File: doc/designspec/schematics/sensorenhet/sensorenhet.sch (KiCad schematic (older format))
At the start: 10 parts, among them IC1 ATMEGA1284P-P, U1 IQEXO-3, U2 Terminator-CTRL, U3 USB-UART, U4 Lidar_Lite_v2, U5 IR-Sensor, U6 IR-Sensor, U7 IR-Sensor

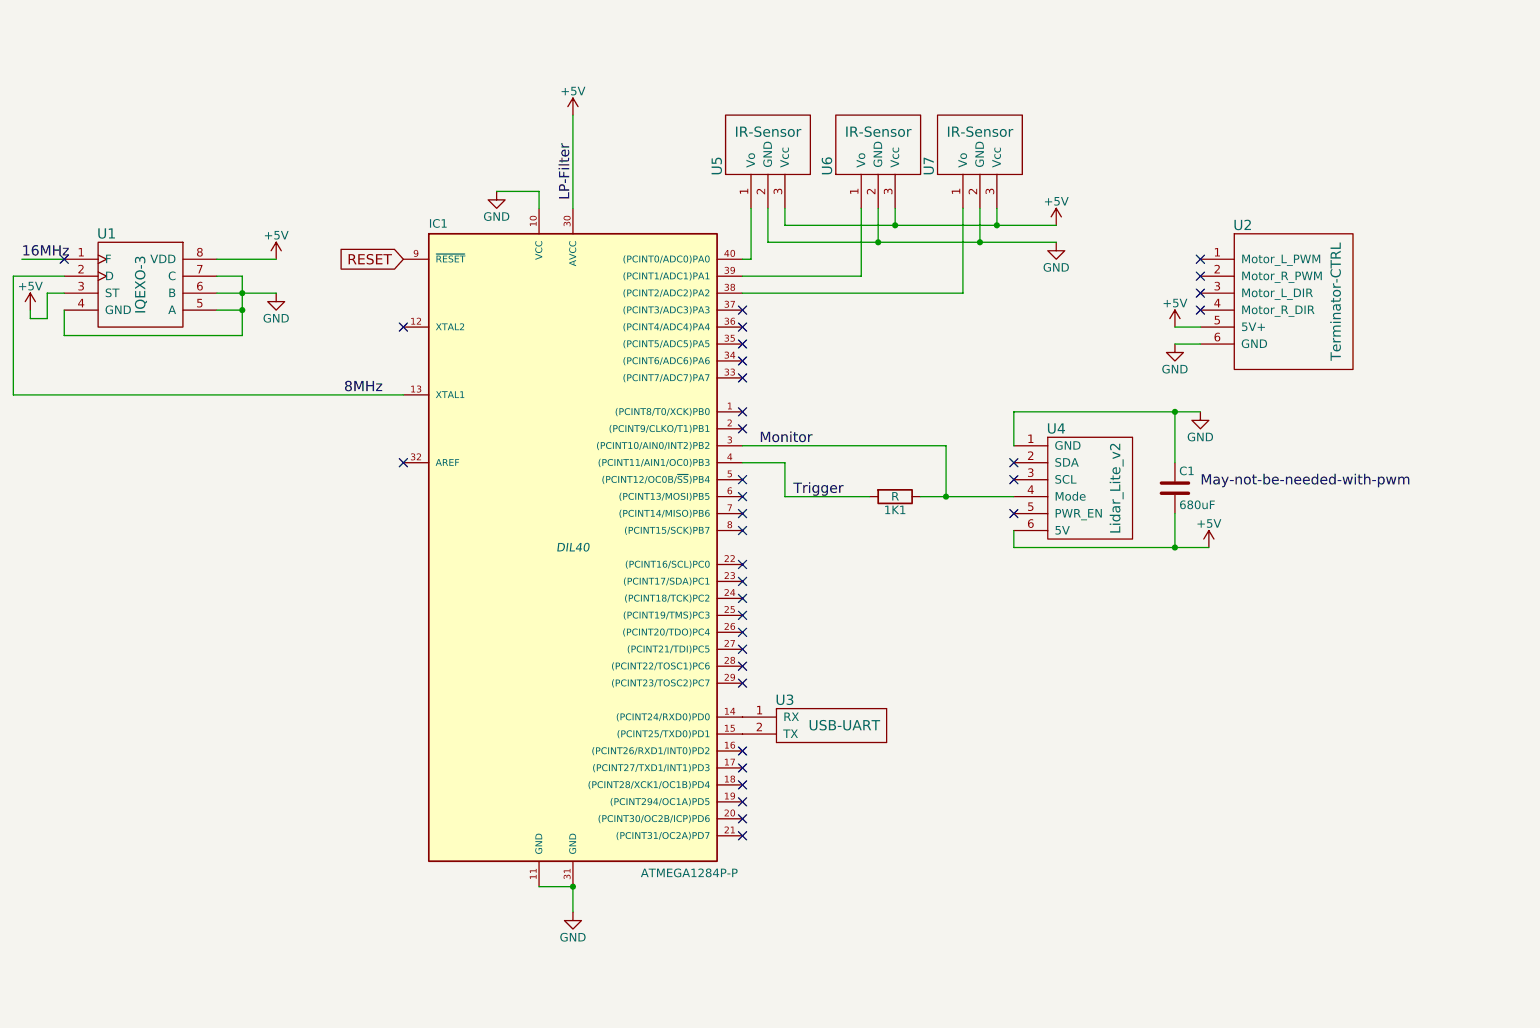
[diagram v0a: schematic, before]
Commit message: Add two more IR sensors
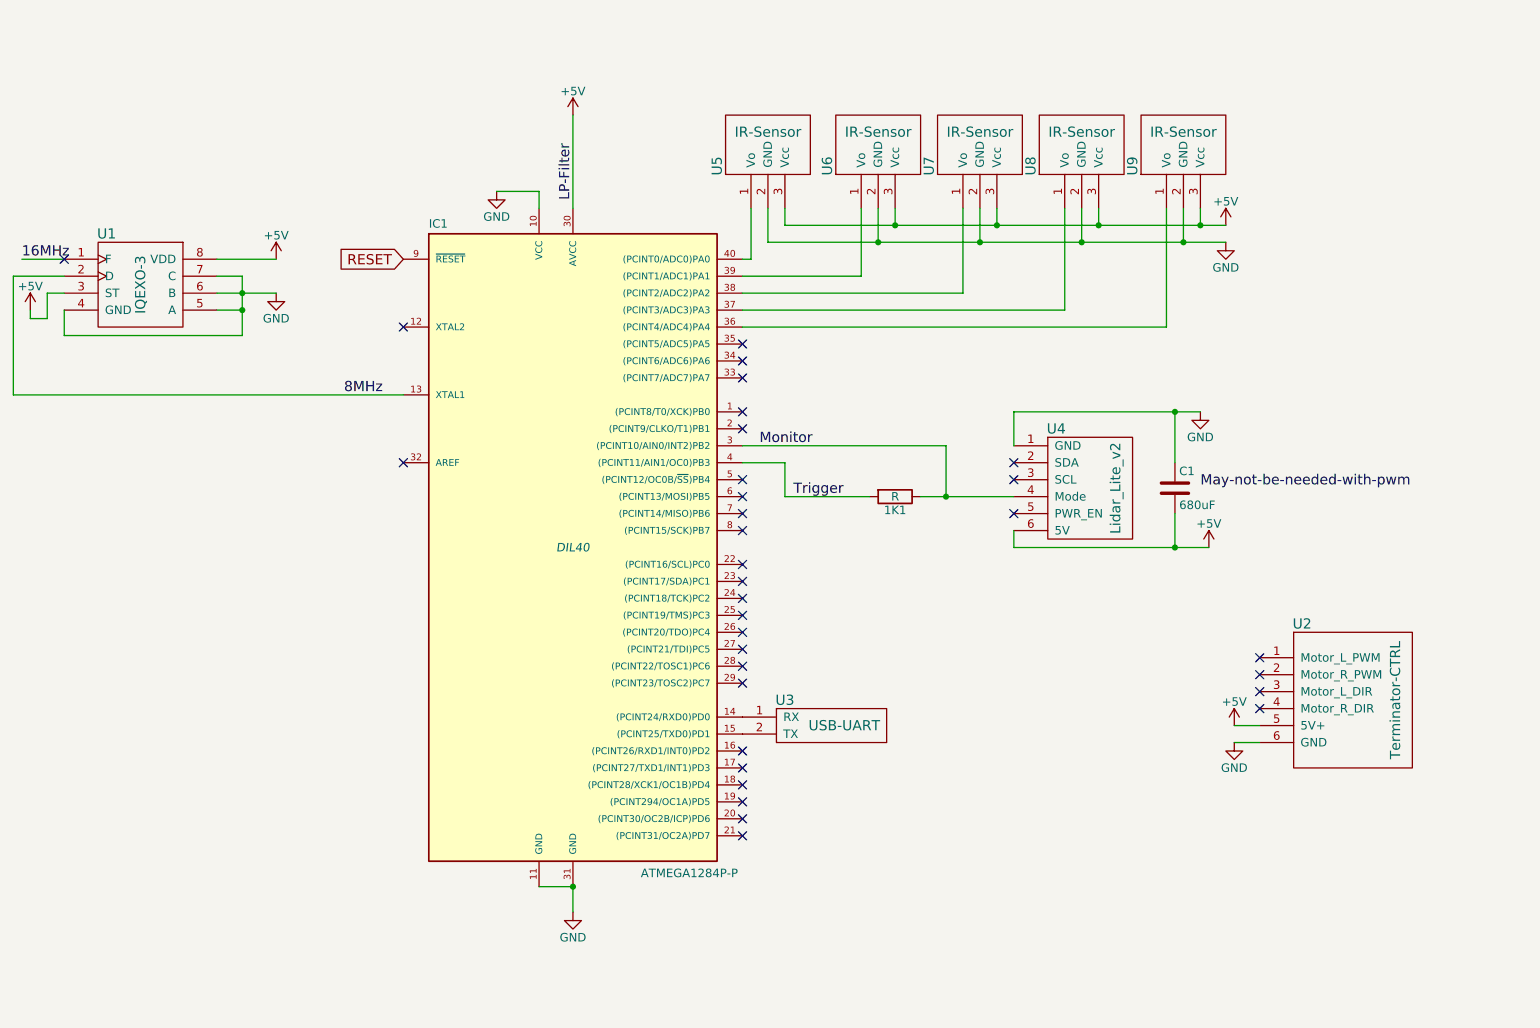
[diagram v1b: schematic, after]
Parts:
- added U8, U9: IR-Sensor, symbol IR-Sensor
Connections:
- net +5V: now also U8.3 (Vcc), U9.3 (Vcc)
- net GND: now also U8.2 (GND), U9.2 (GND)
- net at IC1.36 ((PCINT4/ADC4)PA4): now also U9.1 (Vo)
- net at IC1.37 ((PCINT3/ADC3)PA3): now also U8.1 (Vo)
- no-connect marks 35 -> 33
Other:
- moved on the sheet: U2
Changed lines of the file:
@@
 LIBS:valves
 LIBS:tsea29
+LIBS:sensorenhet-cache
 EELAYER 25 0
 EELAYER END
@@
 RESET
 NoConn ~ 1750 2000
-NoConn ~ 5750 2400
 NoConn ~ 5750 2500
 NoConn ~ 5750 2600
@@
 L Terminator-CTRL U2
 U 1 1 57FA7BA2
-P 9250 2200
-F 0 "U2" H 8700 2600 60  0000 C CNN
-F 1 "Terminator-CTRL" V 9250 2150 60  0000 C CNN
-F 2 "" H 9250 2200 60  0001 C CNN
-F 3 "" H 9250 2200 60  0001 C CNN
-	1    9250 2200
-	1    0    0    -1
-$EndComp
-NoConn ~ 8450 2000
-NoConn ~ 8450 2100
-NoConn ~ 8450 2200
-NoConn ~ 8450 2300
+P 9600 4550
+F 0 "U2" H 9050 4950 60  0000 C CNN
+F 1 "Terminator-CTRL" V 9600 4500 60  0000 C CNN
+F 2 "" H 9600 4550 60  0001 C CNN
+F 3 "" H 9600 4550 60  0001 C CNN
+	1    9600 4550
+	1    0    0    -1
+$EndComp
+NoConn ~ 8800 4350
+NoConn ~ 8800 4450
+NoConn ~ 8800 4550
+NoConn ~ 8800 4650
 $Comp
 L +5V #PWR07
 U 1 1 57FA7CB1
-P 8300 2400
-F 0 "#PWR07" H 8300 2250 50  0001 C CNN
-F 1 "+5V" H 8300 2540 50  0000 C CNN
-F 2 "" H 8300 2400 50  0000 C CNN
-F 3 "" H 8300 2400 50  0000 C CNN
-	1    8300 2400
+P 8650 4750
+F 0 "#PWR07" H 8650 4600 50  0001 C CNN
+F 1 "+5V" H 8650 4890 50  0000 C CNN
+F 2 "" H 8650 4750 50  0000 C CNN
+F 3 "" H 8650 4750 50  0000 C CNN
+	1    8650 4750
 	1    0    0    -1
 $EndComp
@@
 L GND #PWR08
 U 1 1 57FA7CCD
-P 8300 2500
-F 0 "#PWR08" H 8300 2250 50  0001 C CNN
-F 1 "GND" H 8300 2350 50  0000 C CNN
-F 2 "" H 8300 2500 50  0000 C CNN
-F 3 "" H 8300 2500 50  0000 C CNN
-	1    8300 2500
+P 8650 4850
+F 0 "#PWR08" H 8650 4600 50  0001 C CNN
+F 1 "GND" H 8650 4700 50  0000 C CNN
+F 2 "" H 8650 4850 50  0000 C CNN
+F 3 "" H 8650 4850 50  0000 C CNN
+	1    8650 4850
 	1    0    0    -1
 $EndComp
@@
 	0    -1   -1   0
 $EndComp
+$Comp
+L +5V #PWR011
+U 1 1 57FA9432
+P 8600 1800
+F 0 "#PWR011" H 8600 1650 50  0001 C CNN
+F 1 "+5V" H 8600 1940 50  0000 C CNN
+F 2 "" H 8600 1800 50  0000 C CNN
+F 3 "" H 8600 1800 50  0000 C CNN
+	1    8600 1800
+	1    0    0    -1
+$EndComp
+$Comp
+L GND #PWR012
+U 1 1 57FA945C
+P 8600 1900
+F 0 "#PWR012" H 8600 1650 50  0001 C CNN
+F 1 "GND" H 8600 1750 50  0000 C CNN
+F 2 "" H 8600 1900 50  0000 C CNN
+F 3 "" H 8600 1900 50  0000 C CNN
+	1    8600 1900
+	1    0    0    -1
+$EndComp
+$Comp
+L IR-Sensor U8
+U 1 1 57FD3F03
+P 7750 1250
+F 0 "U8" H 7550 1550 60  0000 C CNN
+F 1 "IR-Sensor" V 7750 1250 60  0000 C CNN
+F 2 "" H 7750 1250 60  0001 C CNN
+F 3 "" H 7750 1250 60  0001 C CNN
+	1    7750 1250
+	0    -1   -1   0
+$EndComp
+$Comp
+L IR-Sensor U9
+U 1 1 57FD3F5C
+P 8350 1250
+F 0 "U9" H 8150 1550 60  0000 C CNN
+F 1 "IR-Sensor" V 8350 1250 60  0000 C CNN
+F 2 "" H 8350 1250 60  0001 C CNN
+F 3 "" H 8350 1250 60  0001 C CNN
+	1    8350 1250
+	0    -1   -1   0
+$EndComp
 Wire Wire Line
 	4750 1150 4750 1700
@@
 	2800 2300 2650 2300
 Wire Wire Line
-	2800 2100 2800 2200
-Wire Wire Line
-	2800 2200 2800 2300
-Wire Wire Line
-	2800 2300 2800 2450
-Wire Wire Line
-	2650 2200 2800 2200
-Wire Wire Line
-	2800 2200 3000 2200
+	2800 2100 2800 2450
+Wire Wire Line
+	2650 2200 3000 2200
 Connection ~ 2800 2200
 Wire Wire Line
@@
 	1550 2350 1550 2300
 Wire Wire Line
-	8450 2500 8300 2500
-Wire Wire Line
-	8450 2400 8300 2400
-Wire Wire Line
-	7350 3700 8300 3700
-Wire Wire Line
-	8300 3700 8500 3700
+	8800 4850 8650 4850
+Wire Wire Line
+	8800 4750 8650 4750
+Wire Wire Line
+	7350 3700 8500 3700
 Wire Wire Line
 	7350 3700 7350 3600
 Wire Wire Line
-	7350 2900 8300 2900
-Wire Wire Line
-	8300 2900 8450 2900
+	7350 2900 8450 2900
 Wire Wire Line
 	7350 2900 7350 3100
@@
 	6000 3400 6500 3400
 Wire Wire Line
-	6800 3400 6950 3400
-Wire Wire Line
-	6950 3400 7350 3400
+	6800 3400 7350 3400
 Connection ~ 6950 3400
 Wire Wire Line
@@
 	5900 1700 5900 1900
 Wire Wire Line
-	5900 1900 6550 1900
-Wire Wire Line
-	6550 1900 7150 1900
-Wire Wire Line
-	7150 1900 7600 1900
+	5900 1900 8600 1900
 Wire Wire Line
 	7150 1700 7150 1900
@@
 	6000 1700 6000 1800
 Wire Wire Line
-	6000 1800 6650 1800
-Wire Wire Line
-	6650 1800 7250 1800
-Wire Wire Line
-	7250 1800 7600 1800
+	6000 1800 8600 1800
 Wire Wire Line
 	7250 1700 7250 1800
@@
 	6650 1700 6650 1800
 Connection ~ 6650 1800
-$Comp
-L +5V #PWR011
-U 1 1 57FA9432
-P 7600 1800
-F 0 "#PWR011" H 7600 1650 50  0001 C CNN
-F 1 "+5V" H 7600 1940 50  0000 C CNN
-F 2 "" H 7600 1800 50  0000 C CNN
-F 3 "" H 7600 1800 50  0000 C CNN
-	1    7600 1800
-	1    0    0    -1
-$EndComp
-$Comp
-L GND #PWR012
-U 1 1 57FA945C
-P 7600 1900
-F 0 "#PWR012" H 7600 1650 50  0001 C CNN
-F 1 "GND" H 7600 1750 50  0000 C CNN
-F 2 "" H 7600 1900 50  0000 C CNN
-F 3 "" H 7600 1900 50  0000 C CNN
-	1    7600 1900
-	1    0    0    -1
-$EndComp
-NoConn ~ 5750 2300
+Wire Wire Line
+	8450 1700 8450 1800
+Connection ~ 8450 1800
+Wire Wire Line
+	8350 1700 8350 1900
+Connection ~ 8350 1900
+Wire Wire Line
+	8250 1700 8250 2400
+Wire Wire Line
+	8250 2400 5750 2400
+Wire Wire Line
+	5750 2300 7650 2300
+Wire Wire Line
+	7650 2300 7650 1700
+Wire Wire Line
+	7750 1700 7750 1900
+Connection ~ 7750 1900
+Wire Wire Line
+	7850 1700 7850 1800
+Connection ~ 7850 1800
 $EndSCHEMATC

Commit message: Add gyro
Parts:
- added C2, C3: 1uF, symbol C
- added C4: 0.1uF, symbol C
- added C5: C, symbol C
- added U10: MLX90609, symbol MLX90609
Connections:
- net +5V: now also C2.1, C3.1, U10.~ (VSSA)
- net GND: now also C2.2, C3.2, C4.2, U10.~ (VSSA)
- net OUTAR: now reaches IC1.35 ((PCINT5/ADC5)PA5)
- net OUTAR: now also C5.1, U10.~ (VSSA)
- new net: C4.1, U10.~ (VSSA)
- new net: C5.2, U10.~ (VSSA)
- no-connect marks 33 -> 40
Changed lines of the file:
@@
 RESET
 NoConn ~ 1750 2000
-NoConn ~ 5750 2500
 NoConn ~ 5750 2600
 NoConn ~ 5750 2700
@@
 $EndComp
 $Comp
-L USB-UART U3
-U 1 1 57F7998E
-P 6350 4750
-F 0 "U3" H 6000 4900 60  0000 C CNN
-F 1 "USB-UART" H 6350 4750 60  0000 C CNN
-F 2 "" H 6350 4750 60  0001 C CNN
-F 3 "" H 6350 4750 60  0001 C CNN
-	1    6350 4750
-	1    0    0    -1
-$EndComp
-$Comp
 L Terminator-CTRL U2
 U 1 1 57FA7BA2
@@
 	0    -1   -1   0
 $EndComp
+$Comp
+L USB-UART U3
+U 1 1 57F7998E
+P 6350 4750
+F 0 "U3" H 6000 4900 60  0000 C CNN
+F 1 "USB-UART" H 6350 4750 60  0000 C CNN
+F 2 "" H 6350 4750 60  0001 C CNN
+F 3 "" H 6350 4750 60  0001 C CNN
+	1    6350 4750
+	1    0    0    -1
+$EndComp
+$Comp
+L +5V #PWR013
+U 1 1 57FD4853
+P 6550 5600
+F 0 "#PWR013" H 6550 5450 50  0001 C CNN
+F 1 "+5V" H 6550 5740 50  0000 C CNN
+F 2 "" H 6550 5600 50  0000 C CNN
+F 3 "" H 6550 5600 50  0000 C CNN
+	1    6550 5600
+	1    0    0    -1
+$EndComp
+$Comp
+L C C2
+U 1 1 57FD4A5E
+P 6900 5500
+F 0 "C2" H 6925 5600 50  0000 L CNN
+F 1 "1uF" H 6925 5400 50  0000 L CNN
+F 2 "" H 6938 5350 50  0000 C CNN
+F 3 "" H 6900 5500 50  0000 C CNN
+	1    6900 5500
+	1    0    0    -1
+$EndComp
+$Comp
+L GND #PWR014
+U 1 1 57FD4C6E
+P 6550 6250
+F 0 "#PWR014" H 6550 6000 50  0001 C CNN
+F 1 "GND" H 6550 6100 50  0000 C CNN
+F 2 "" H 6550 6250 50  0000 C CNN
+F 3 "" H 6550 6250 50  0000 C CNN
+	1    6550 6250
+	1    0    0    -1
+$EndComp
+$Comp
+L C C3
+U 1 1 57FD4CFD
+P 7000 5950
+F 0 "C3" H 7025 6050 50  0000 L CNN
+F 1 "1uF" H 7025 5850 50  0000 L CNN
+F 2 "" H 7038 5800 50  0000 C CNN
+F 3 "" H 7000 5950 50  0000 C CNN
+	1    7000 5950
+	1    0    0    -1
+$EndComp
 Wire Wire Line
 	4750 1150 4750 1700
@@
 	7850 1700 7850 1800
 Connection ~ 7850 1800
+Wire Wire Line
+	6650 5350 7500 5350
+Wire Wire Line
+	6650 5350 6650 5800
+Wire Wire Line
+	6650 5600 6550 5600
+Wire Wire Line
+	7500 5450 7400 5450
+Wire Wire Line
+	7400 5450 7400 5650
+Wire Wire Line
+	7400 5650 7150 5650
+Wire Wire Line
+	7150 5800 7150 5650
+Wire Wire Line
+	6650 5800 7150 5800
+Connection ~ 6650 5600
+Wire Wire Line
+	6900 5650 6900 6250
+Wire Wire Line
+	6550 6250 7500 6250
+Wire Wire Line
+	7000 6250 7000 6100
+Connection ~ 6900 6250
+Wire Wire Line
+	7500 5650 7500 5800
+Wire Wire Line
+	7500 5800 7200 5800
+$Comp
+L C C4
+U 1 1 57FD504A
+P 7200 5950
+F 0 "C4" H 7225 6050 50  0000 L CNN
+F 1 "0.1uF" H 7225 5850 50  0000 L CNN
+F 2 "" H 7238 5800 50  0000 C CNN
+F 3 "" H 7200 5950 50  0000 C CNN
+	1    7200 5950
+	1    0    0    -1
+$EndComp
+Wire Wire Line
+	7200 6250 7200 6100
+Connection ~ 7000 6250
+Wire Wire Line
+	7500 6050 7450 6050
+Wire Wire Line
+	7450 6050 7450 6250
+Connection ~ 7200 6250
+Wire Wire Line
+	7500 6150 7450 6150
+Connection ~ 7450 6150
+Connection ~ 7450 6250
+NoConn ~ 8650 5350
+NoConn ~ 8650 5450
+NoConn ~ 8650 5550
+NoConn ~ 8650 5650
+NoConn ~ 8650 5750
+NoConn ~ 8650 5850
+$Comp
+L MLX90609 U10
+U 1 1 57FD56B0
+P 8150 5750
+F 0 "U10" H 7750 6250 60  0000 C CNN
+F 1 "MLX90609" V 8050 5750 60  0000 C CNN
+F 2 "" H 8150 5750 60  0001 C CNN
+F 3 "" H 8150 5750 60  0001 C CNN
+	1    8150 5750
+	1    0    0    -1
+$EndComp
+NoConn ~ 8650 5950
+Text Label 8700 6000 0    60   ~ 0
+VREF>Atmega?
+NoConn ~ 8650 6050
+$Comp
+L C C5
+U 1 1 57FD58C6
+P 9550 6050
+F 0 "C5" H 9575 6150 50  0000 L CNN
+F 1 "C" H 9575 5950 50  0000 L CNN
+F 2 "" H 9588 5900 50  0000 C CNN
+F 3 "" H 9550 6050 50  0000 C CNN
+	1    9550 6050
+	1    0    0    -1
+$EndComp
+Wire Wire Line
+	8650 6250 9550 6250
+Wire Wire Line
+	9550 6250 9550 6200
+Wire Wire Line
+	8650 6150 9400 6150
+Wire Wire Line
+	9400 6150 9400 5900
+Wire Wire Line
+	9400 5900 9900 5900
+Connection ~ 9550 5900
+Text GLabel 9900 5900 2    60   Input ~ 0
+OUTAR
+Text GLabel 5750 2500 2    60   Input ~ 0
+OUTAR
+Connection ~ 6900 5350
+Connection ~ 7000 5800
 $EndSCHEMATC

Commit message: Add JTAG programmer
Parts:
- added CON?: AVR-JTAG-10, AVR-JTAG-10, symbol AVR-JTAG-10
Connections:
- net at IC1.24 ((PCINT18/TCK)PC2): now also CON?.1
- net at IC1.25 ((PCINT19/TMS)PC3): now also CON?.5
- net at IC1.26 ((PCINT20/TDO)PC4): now also CON?.3
- net at IC1.27 ((PCINT21/TDI)PC5): now also CON?.9
- no-connect marks 40 -> 36
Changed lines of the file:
@@
 NoConn ~ 5750 3800
 NoConn ~ 5750 3900
-NoConn ~ 5750 4000
-NoConn ~ 5750 4100
-NoConn ~ 5750 4200
-NoConn ~ 5750 4300
 NoConn ~ 5750 4400
 NoConn ~ 5750 4500
@@
 	7400 5650 7150 5650
 Wire Wire Line
-	7150 5800 7150 5650
-Wire Wire Line
-	6650 5800 7150 5800
+	7150 5650 7150 5800
+Wire Wire Line
+	7150 5800 6650 5800
 Connection ~ 6650 5600
 Wire Wire Line
@@
 Connection ~ 6900 5350
 Connection ~ 7000 5800
+$Comp
+L AVR-JTAG-10 CON?
+U 1 1 5803B7E6
+P 6850 4150
+F 0 "CON?" H 6680 4480 50  0000 C CNN
+F 1 "AVR-JTAG-10" H 6510 3820 50  0000 L BNN
+F 2 "AVR-JTAG-10" V 6280 4170 50  0001 C CNN
+F 3 "" H 6850 4150 50  0000 C CNN
+	1    6850 4150
+	1    0    0    -1
+$EndComp
+Wire Wire Line
+	6650 3950 6050 3950
+Wire Wire Line
+	6050 3950 6050 4000
+Wire Wire Line
+	6050 4000 5750 4000
+Wire Wire Line
+	5750 4100 6050 4100
+Wire Wire Line
+	6050 4100 6050 4150
+Wire Wire Line
+	6050 4150 6650 4150
+Wire Wire Line
+	6650 4350 6050 4350
+Wire Wire Line
+	6050 4350 6050 4300
+Wire Wire Line
+	6050 4300 5750 4300
+Wire Wire Line
+	5750 4200 6200 4200
+Wire Wire Line
+	6200 4200 6200 4050
+Wire Wire Line
+	6200 4050 6650 4050
 $EndSCHEMATC

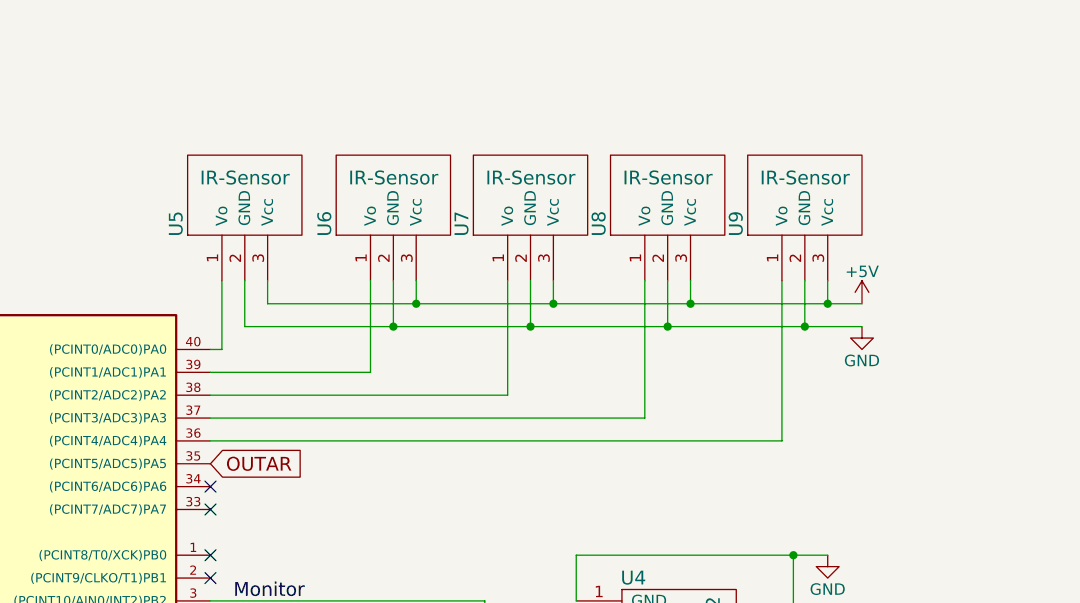
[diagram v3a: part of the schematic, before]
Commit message: Add LP-Filter to IR sensors
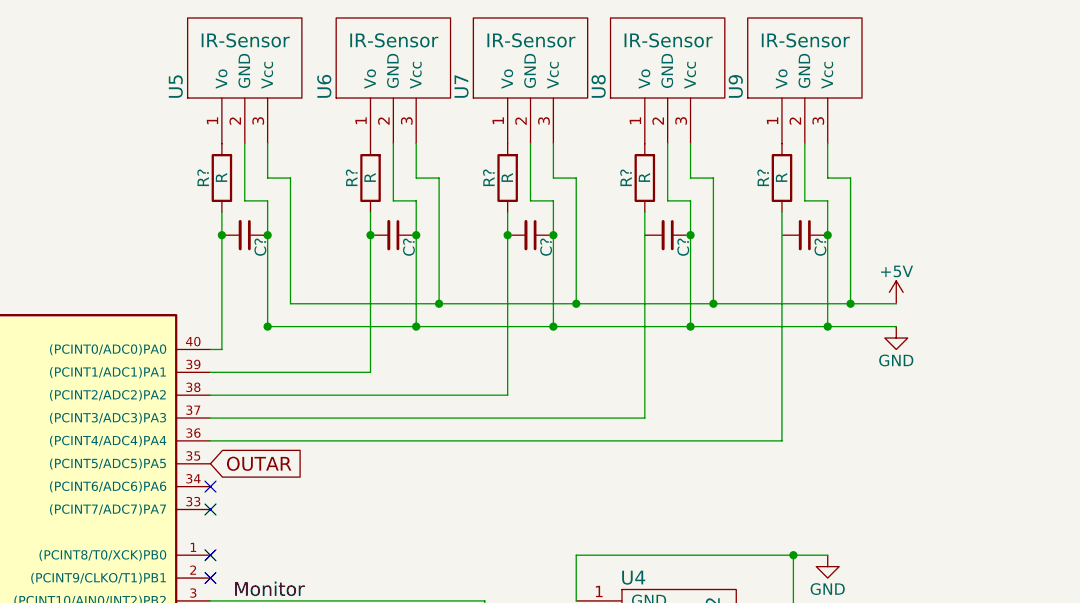
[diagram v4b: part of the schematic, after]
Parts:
- added C? (x5): C_Small, symbol C_Small
- added R? (x5): R, symbol R
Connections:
- net GND: now also C?.1, C?.1, C?.1, C?.1, C?.1
- net at IC1.36 ((PCINT4/ADC4)PA4): now also R?.1; no longer U9.1 (Vo)
- net at IC1.37 ((PCINT3/ADC3)PA3): now also R?.1; no longer U8.1 (Vo)
- net at IC1.38 ((PCINT2/ADC2)PA2): now also C?.2, R?.1; no longer U7.1 (Vo)
- net at IC1.39 ((PCINT1/ADC1)PA1): now also C?.2, R?.1; no longer U6.1 (Vo)
- net at IC1.40 ((PCINT0/ADC0)PA0): now also C?.2, R?.1; no longer U5.1 (Vo)
- new net: R?.2, U6.1 (Vo)
- new net: R?.2, U7.1 (Vo)
- new net: R?.2, U5.1 (Vo)
- new net: R?.2, U8.1 (Vo)
- new net: R?.2, U9.1 (Vo)
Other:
- moved on the sheet: U5, U6, U7, U8, U9
